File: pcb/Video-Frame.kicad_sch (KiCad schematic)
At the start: 121 parts, among them J1 POWER, J2 USB_B_Micro, J3 DBG_SWD, J4 Micro_SD_Card_Det, J5 DISPLAY, J6 USART3, SW1 BOOT, SW2 RESET, U1 MP2451DT, U2 SY6280A, U3 SY6280A, U4 HT7533-1, U5 USBLC6-2SC6, U6 STM32F405RGT6, Y1 8MHz, Y2 32.768KHz

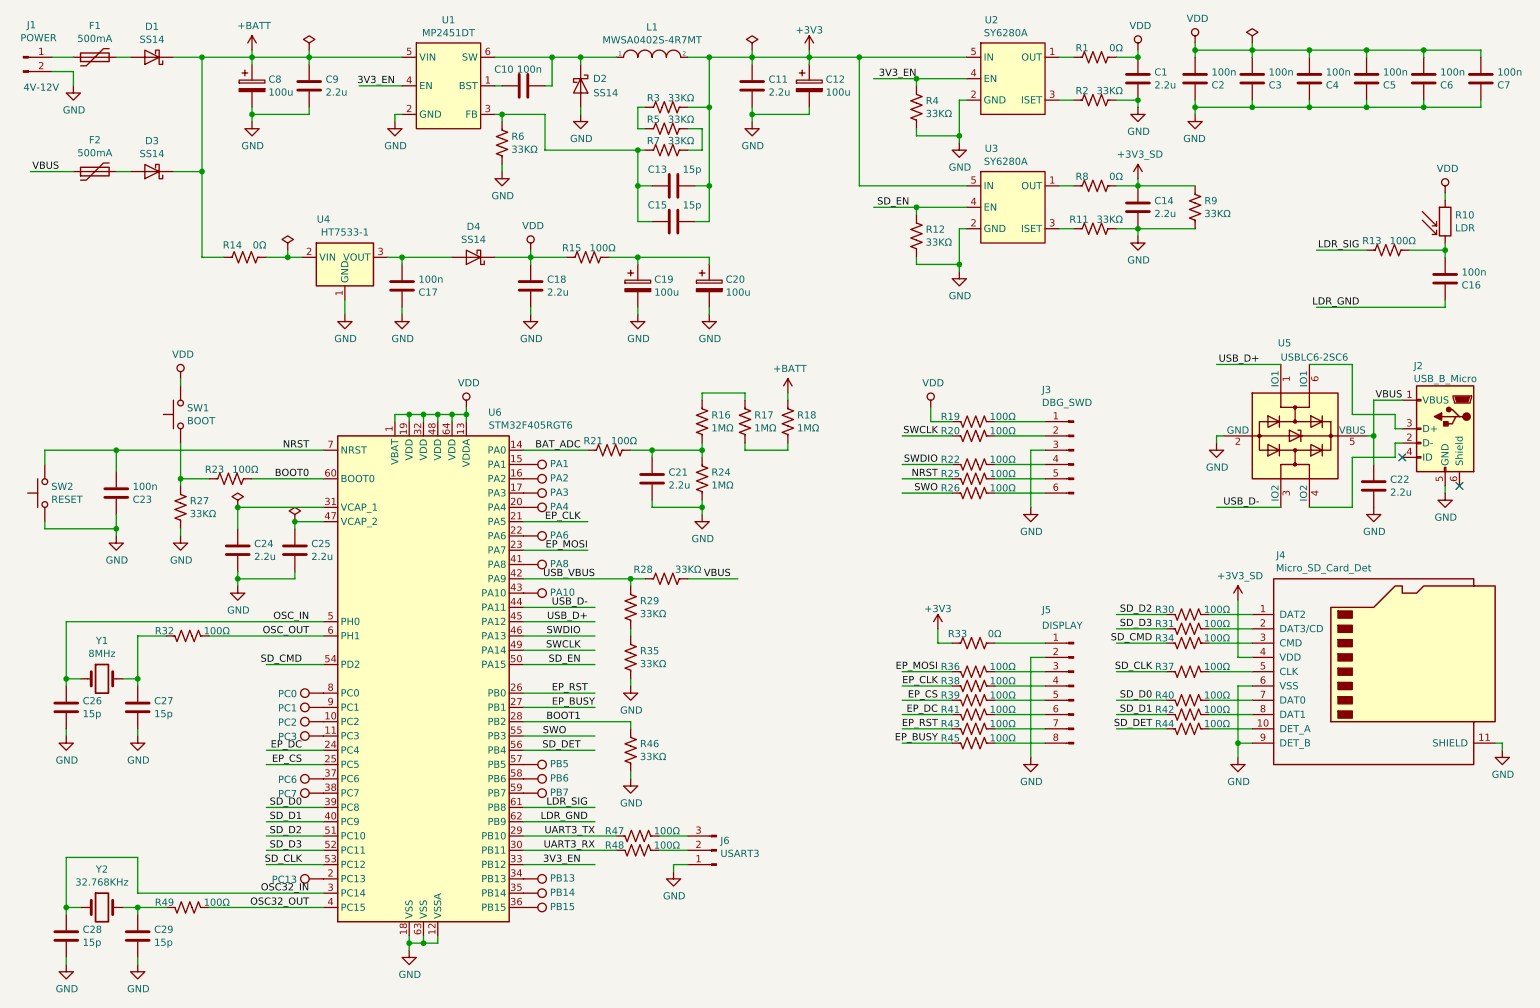
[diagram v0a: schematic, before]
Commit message: PCB Layout
Changes in schematic
+ Fixed +3V3_SD Power NET
+ Changed 100uF electrolytic to 10uF tantalum (lower leakage current)
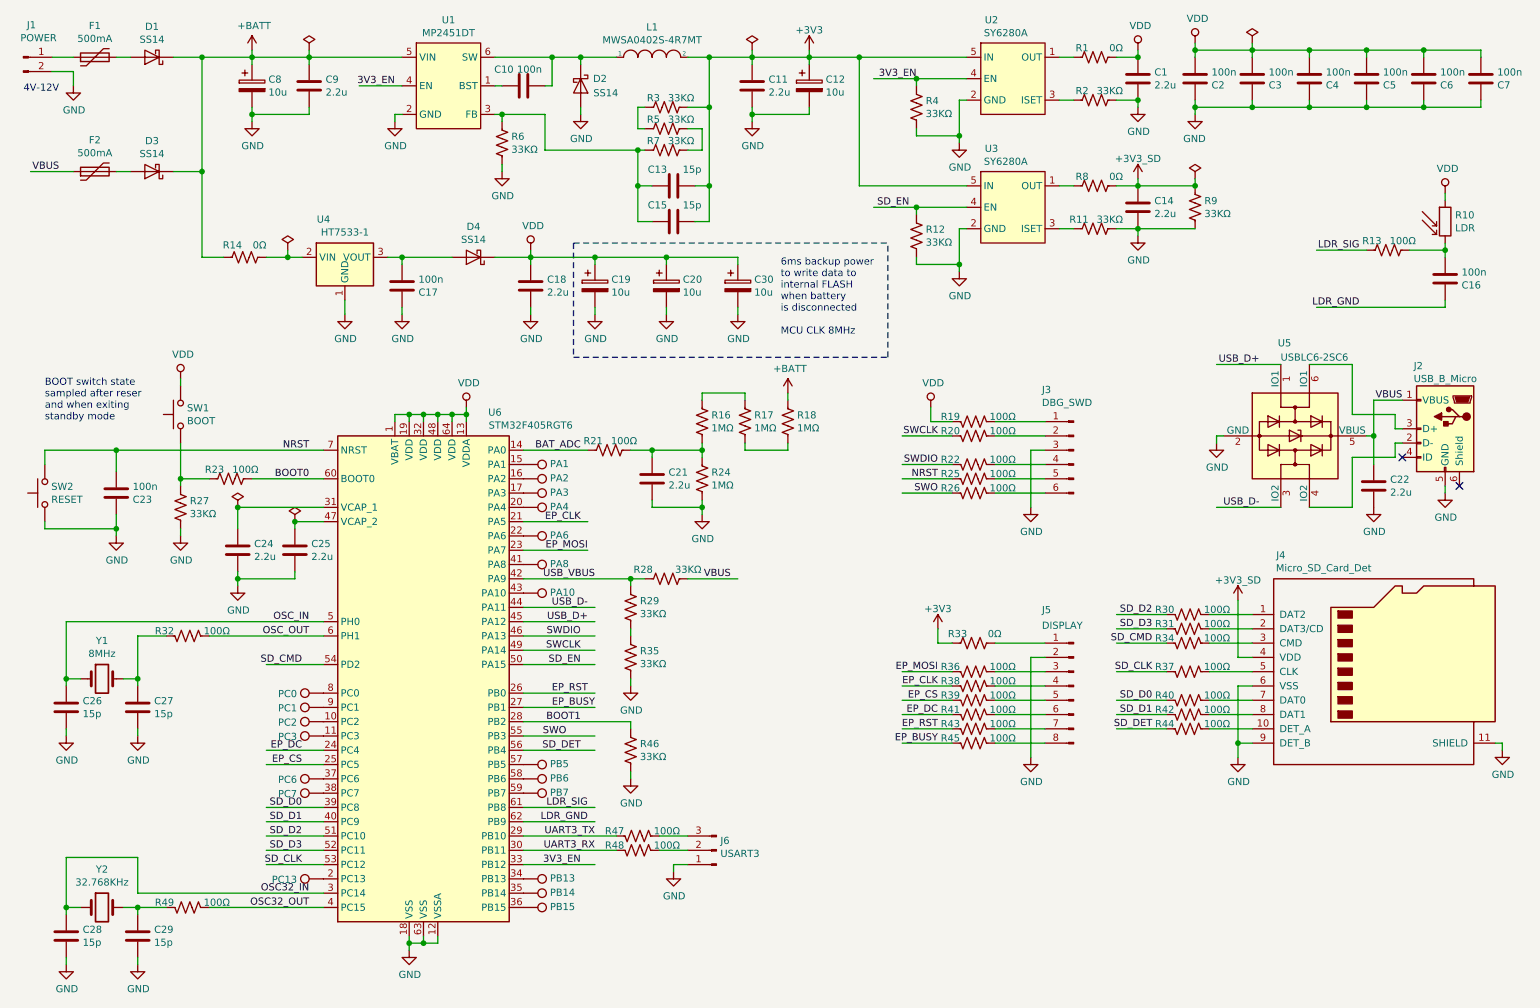
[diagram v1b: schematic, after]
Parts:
- removed R15: 100Ω, Resistor_SMD:R_0603_1608Metric, symbol Device:R_US
- added C30: 10u, Capacitor_Tantalum_SMD:CP_EIA-3216-10_Kemet-I, symbol Device:CP
- C12, C19, C20, C8: value 100u -> 10u; footprint Capacitor_SMD:CP_Elec_6.3x5.3 -> Capacitor_Tantalum_SMD:CP_EIA-3216-10_Kemet-I; LCSC C134723 -> C7171; LCSC Footprint SMD-ECAP-6.3x5.3 -> CASE-A_3216
- F1, F2: LCSC C151168 -> C269127
- J2: footprint Connector_USB:USB_Micro-B_Wuerth_629105150521 -> Connector_MicroUSB:USB_Micro-B_CUI_Devices-UJ2-MIBH-G-SMT-TR
- Y2: LCSC C48615 -> C32346
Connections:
- net +3V3: no longer C14.1, J4.4 (VDD), R8.2, R9.1
- net GND: now also C30.2
- net VDD: now also C19.1, C20.1, C30.1
- new net +3V3_SD: C14.1, J4.4 (VDD), R8.2, R9.1
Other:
- note added: "6ms backup power to write data to internal FLASH when battery is disconnected MCU CLK 8MHz"
- note added: "BOOT switch state sampled after reser and when exiting standby mode"
- moved on the sheet: C19, C20

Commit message: Updated schematic and PCB Layout
Changes in schematic
+ Added super capacitor on VDD
+ Added notes
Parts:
- added C31: 47m, Capacitor_SMD:CP_Elec_10x7.7, symbol Device:CP
- added R15: 100Ω, Resistor_SMD:R_0603_1608Metric, symbol Device:R_US
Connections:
- net GND: now also C31.2
- net VDD: now also R15.1
- new net: C31.1, R15.2
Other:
- note added: "24min @4uA + 10ms @10mA backup power to write data to internal FLASH when battery is disconnected MCU CLK 8MHz"
- note added: "Light Dependent Resistor display not visible when R > 100KΩ -> T > 10ms"
- note removed: "6ms backup power to write data to internal FLASH when battery is disconnected MCU CLK 8MHz"
- moved on the sheet: C17, C18, C19, C20, C30, D4, R14, U4

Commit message: Fixed 100 Ohm resistors part number
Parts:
- R13, R15, R19, R20, R21, R22, R23, R25, R26, R30, R31, R32, R34, R36, R37, R38, R39, R40, R41, R42, R43, R44, R45, R47, R48, R49: LCSC C7250 -> C22775
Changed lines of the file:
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@@
       (effects (font (size 1.27 1.27)) hide)
     )
-    (property "LCSC" "C7250" (id 4) (at 44.45 133.35 0)
+    (property "LCSC" " C22775" (id 4) (at 44.45 133.35 0)
       (effects (font (size 1.27 1.27)) hide)
     )
@@
       (effects (font (size 1.27 1.27)) hide)
     )
-    (property "LCSC" "C7250" (id 4) (at 44.45 181.61 0)
+    (property "LCSC" " C22775" (id 4) (at 44.45 181.61 0)
       (effects (font (size 1.27 1.27)) hide)
     )
@@
       (effects (font (size 1.27 1.27)) hide)
     )
-    (property "LCSC" "C7250" (id 4) (at 52.07 105.41 0)
+    (property "LCSC" " C22775" (id 4) (at 52.07 105.41 0)
       (effects (font (size 1.27 1.27)) hide)
     )
@@
       (effects (font (size 1.27 1.27)) hide)
     )
-    (property "LCSC" "C7250" (id 4) (at 119.38 100.33 0)
+    (property "LCSC" " C22775" (id 4) (at 119.38 100.33 0)
       (effects (font (size 1.27 1.27)) hide)
     )
@@
       (effects (font (size 1.27 1.27)) hide)
     )
-    (property "LCSC" "C7250" (id 4) (at 124.46 168.91 0)
+    (property "LCSC" " C22775" (id 4) (at 124.46 168.91 0)
       (effects (font (size 1.27 1.27)) hide)
     )
@@
       (effects (font (size 1.27 1.27)) hide)
     )
-    (property "LCSC" "C7250" (id 4) (at 124.46 171.45 0)
+    (property "LCSC" " C22775" (id 4) (at 124.46 171.45 0)
       (effects (font (size 1.27 1.27)) hide)
     )
@@
       (effects (font (size 1.27 1.27)) hide)
     )
-    (property "LCSC" "C7250" (id 4) (at 125.73 66.04 0)
+    (property "LCSC" " C22775" (id 4) (at 125.73 66.04 0)
       (effects (font (size 1.27 1.27)) hide)
     )
@@
       (effects (font (size 1.27 1.27)) hide)
     )
-    (property "LCSC" "C7250" (id 4) (at 184.15 95.25 0)
+    (property "LCSC" " C22775" (id 4) (at 184.15 95.25 0)
       (effects (font (size 1.27 1.27)) hide)
     )
@@
       (effects (font (size 1.27 1.27)) hide)
     )
-    (property "LCSC" "C7250" (id 4) (at 184.15 97.79 0)
+    (property "LCSC" " C22775" (id 4) (at 184.15 97.79 0)
       (effects (font (size 1.27 1.27)) hide)
     )
@@
       (effects (font (size 1.27 1.27)) hide)
     )
-    (property "LCSC" "C7250" (id 4) (at 184.15 102.87 0)
+    (property "LCSC" " C22775" (id 4) (at 184.15 102.87 0)
       (effects (font (size 1.27 1.27)) hide)
     )
@@
       (effects (font (size 1.27 1.27)) hide)
     )
-    (property "LCSC" "C7250" (id 4) (at 184.15 105.41 0)
+    (property "LCSC" " C22775" (id 4) (at 184.15 105.41 0)
       (effects (font (size 1.27 1.27)) hide)
     )
@@
       (effects (font (size 1.27 1.27)) hide)
     )
-    (property "LCSC" "C7250" (id 4) (at 184.15 107.95 0)
+    (property "LCSC" " C22775" (id 4) (at 184.15 107.95 0)
       (effects (font (size 1.27 1.27)) hide)
     )
@@
       (effects (font (size 1.27 1.27)) hide)
     )
-    (property "LCSC" "C7250" (id 4) (at 184.15 139.7 0)
+    (property "LCSC" " C22775" (id 4) (at 184.15 139.7 0)
       (effects (font (size 1.27 1.27)) hide)
     )
@@
       (effects (font (size 1.27 1.27)) hide)
     )
-    (property "LCSC" "C7250" (id 4) (at 184.15 142.24 0)
+    (property "LCSC" " C22775" (id 4) (at 184.15 142.24 0)
       (effects (font (size 1.27 1.27)) hide)
     )
@@
       (effects (font (size 1.27 1.27)) hide)
     )
-    (property "LCSC" "C7250" (id 4) (at 184.15 144.78 0)
+    (property "LCSC" " C22775" (id 4) (at 184.15 144.78 0)
       (effects (font (size 1.27 1.27)) hide)
     )
@@
       (effects (font (size 1.27 1.27)) hide)
     )
-    (property "LCSC" "C7250" (id 4) (at 184.15 147.32 0)
+    (property "LCSC" " C22775" (id 4) (at 184.15 147.32 0)
       (effects (font (size 1.27 1.27)) hide)
     )
@@
       (effects (font (size 1.27 1.27)) hide)
     )
-    (property "LCSC" "C7250" (id 4) (at 184.15 149.86 0)
+    (property "LCSC" " C22775" (id 4) (at 184.15 149.86 0)
       (effects (font (size 1.27 1.27)) hide)
     )
@@
       (effects (font (size 1.27 1.27)) hide)
     )
-    (property "LCSC" "C7250" (id 4) (at 184.15 152.4 0)
+    (property "LCSC" " C22775" (id 4) (at 184.15 152.4 0)
       (effects (font (size 1.27 1.27)) hide)
     )
@@
       (effects (font (size 1.27 1.27)) hide)
     )
-    (property "LCSC" "C7250" (id 4) (at 222.25 129.54 0)
+    (property "LCSC" " C22775" (id 4) (at 222.25 129.54 0)
       (effects (font (size 1.27 1.27)) hide)
     )
@@
       (effects (font (size 1.27 1.27)) hide)
     )
-    (property "LCSC" "C7250" (id 4) (at 222.25 132.08 0)
+    (property "LCSC" " C22775" (id 4) (at 222.25 132.08 0)
       (effects (font (size 1.27 1.27)) hide)
     )
@@
       (effects (font (size 1.27 1.27)) hide)
     )
-    (property "LCSC" "C7250" (id 4) (at 222.25 134.62 0)
+    (property "LCSC" " C22775" (id 4) (at 222.25 134.62 0)
       (effects (font (size 1.27 1.27)) hide)
     )
@@
       (effects (font (size 1.27 1.27)) hide)
     )
-    (property "LCSC" "C7250" (id 4) (at 222.25 139.7 0)
+    (property "LCSC" " C22775" (id 4) (at 222.25 139.7 0)
       (effects (font (size 1.27 1.27)) hide)
     )
@@
       (effects (font (size 1.27 1.27)) hide)
     )
-    (property "LCSC" "C7250" (id 4) (at 222.25 144.78 0)
+    (property "LCSC" " C22775" (id 4) (at 222.25 144.78 0)
       (effects (font (size 1.27 1.27)) hide)
     )
@@
       (effects (font (size 1.27 1.27)) hide)
     )
-    (property "LCSC" "C7250" (id 4) (at 222.25 147.32 0)
+    (property "LCSC" " C22775" (id 4) (at 222.25 147.32 0)
       (effects (font (size 1.27 1.27)) hide)
     )
@@
       (effects (font (size 1.27 1.27)) hide)
     )
-    (property "LCSC" "C7250" (id 4) (at 222.25 149.86 0)
+    (property "LCSC" " C22775" (id 4) (at 222.25 149.86 0)
       (effects (font (size 1.27 1.27)) hide)
     )
@@
       (effects (font (size 1.27 1.27)) hide)
     )
-    (property "LCSC" "C7250" (id 4) (at 257.81 64.77 0)
-      (effects (font (size 1.27 1.27)) hide)
-    )
+    (property "LCSC" " C22775" (id 4) (at 257.81 64.77 0)
+      (effects (font (size 1.27 1.27)) hide)
+    )
